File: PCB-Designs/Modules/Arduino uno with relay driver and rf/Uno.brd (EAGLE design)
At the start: 157.2 x 94 mm, 54 parts, among them IC1 ATMEGA328, IC2 7805, Q1 12MHZ, T1 BC547, T2 BC547, T3 BC547, T4 BC547

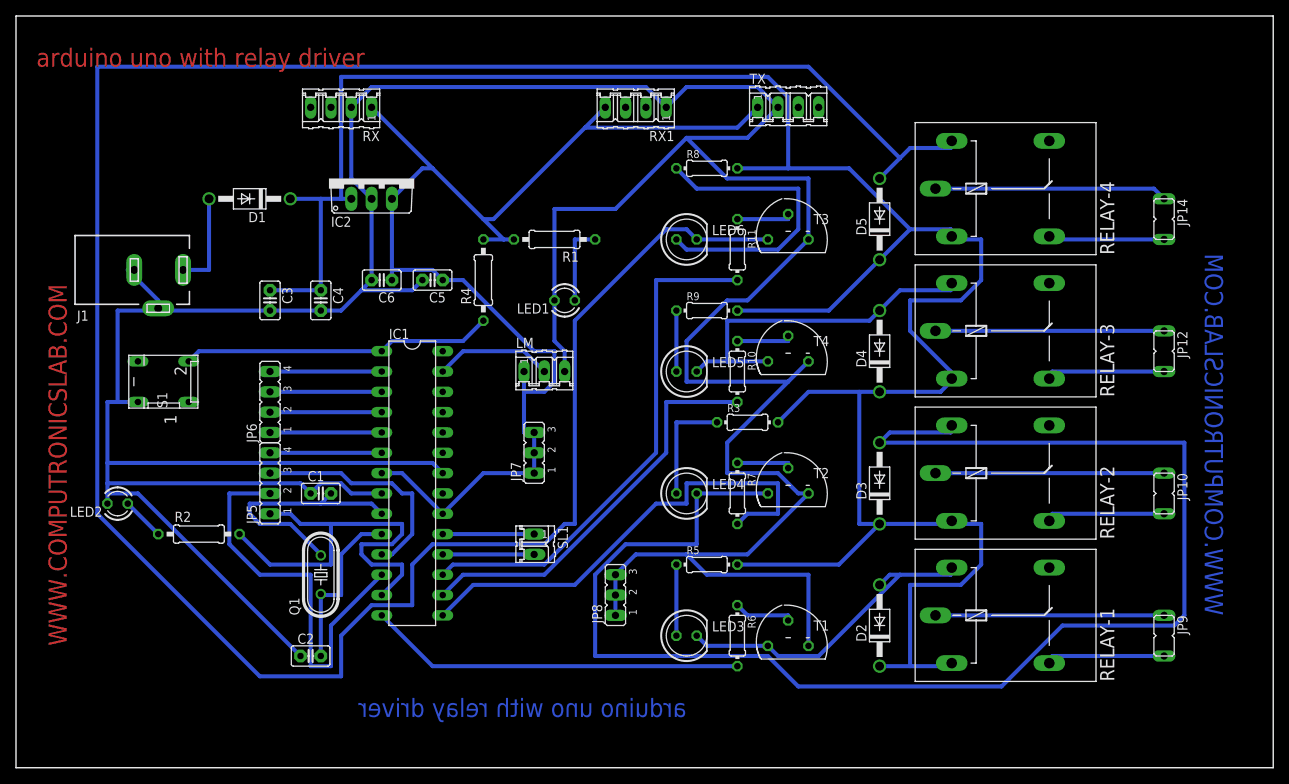
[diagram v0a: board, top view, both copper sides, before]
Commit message: 
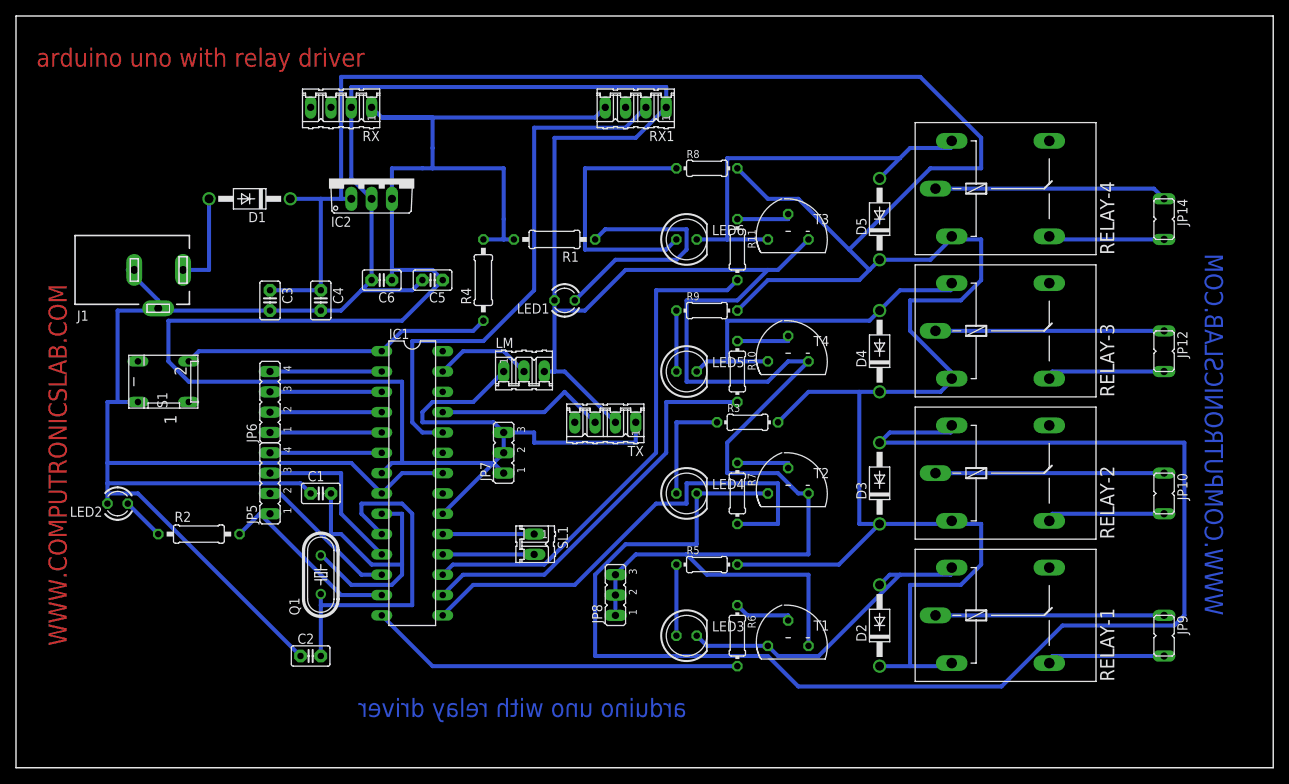
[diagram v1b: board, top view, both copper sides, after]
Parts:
- moved TX 45.5 mm to (77.5, 52.1), turned to 180 degrees
- moved JP7 3.81 mm to (64.8, 48.3)
- moved LM 2.54 mm to (67.3, 58.4)
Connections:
- net N$9: now also RX1.2
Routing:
- net N$58: track 309.1 -> 52.0 mm
- net N$4: track 157.5 -> 246.5 mm
- net N$9: track 0.00 -> 67.7 mm
- net N$7: track 304.2 -> 342.1 mm
- net N$19: track 51.2 -> 18.2 mm
- net N$21: track 53.7 -> 24.3 mm
- net N$11: track 0.00 -> 21.7 mm
- net N$6: track 10.2 -> 31.1 mm
- net N$2: track 21.5 -> 42.3 mm
- net N$20: track 28.8 -> 21.2 mm
- net N$1: track 31.2 -> 38.1 mm
- net N$48: track 38.2 -> 33.5 mm
- net N$55: track 473.2 -> 469.3 mm
- net N$8: track 14.8 -> 12.3 mm
- net N$57: track 64.7 -> 64.0 mm
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
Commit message: 
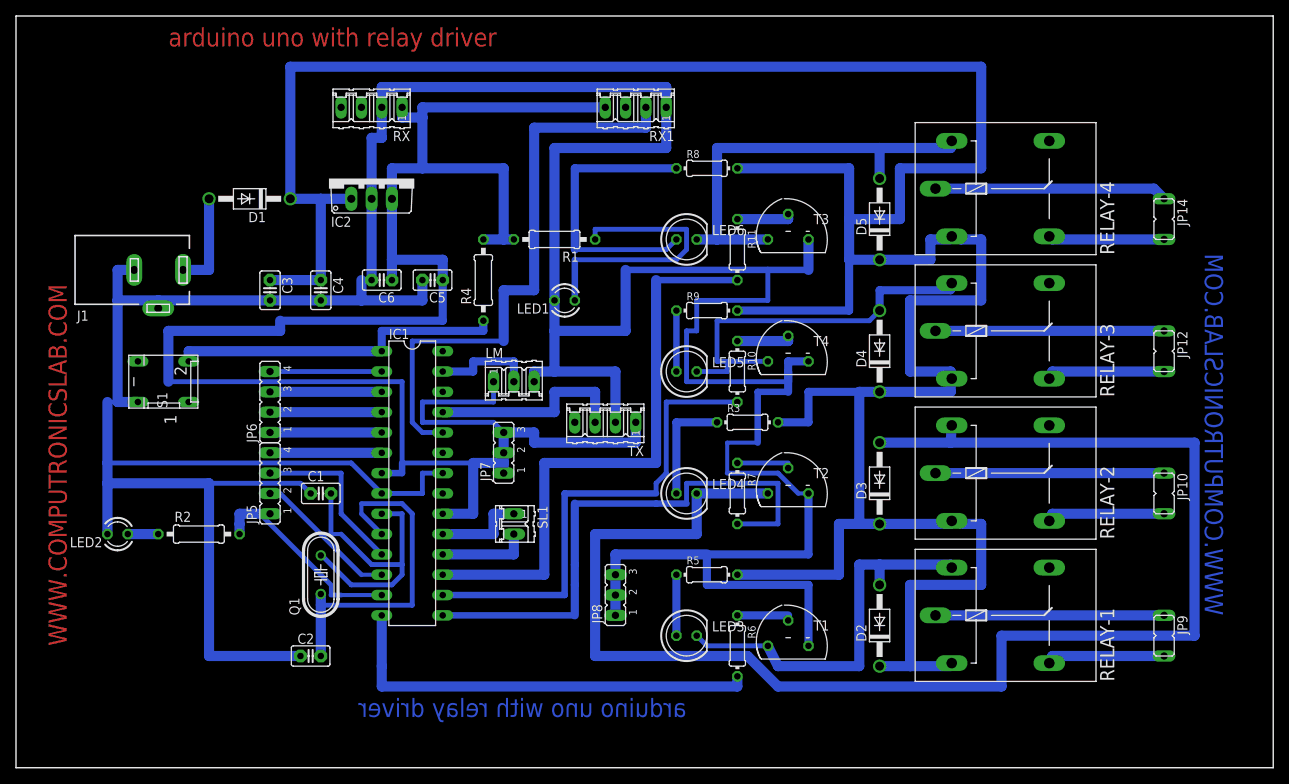
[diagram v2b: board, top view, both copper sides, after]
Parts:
- moved LED2 3.81 mm to (16.5, 38.1)
- moved RX 3.81 mm to (48.3, 91.4)
- moved SL1 3.59 mm to (66.0, 39.4)
- moved LM 1.80 mm to (66.0, 57.1)
- moved R6 1.27 mm to (94.0, 24.1)
- moved C3 1.27 mm to (35.6, 68.6)
- moved C4 1.27 mm to (41.9, 68.6)
- moved R5 1.27 mm to (90.2, 33.0)
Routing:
- net N$7: track 342.1 -> 378.3 mm
- net N$55: track 469.3 -> 497.7 mm
- net N$57: track 64.0 -> 73.7 mm
- net N$56: track 50.5 -> 60.2 mm
- net N$28: track 41.0 -> 49.5 mm
- net N$59: track 60.4 -> 68.6 mm
- net N$41: track 47.1 -> 54.6 mm
- net N$9: track 67.7 -> 72.9 mm
- net N$43: track 44.9 -> 49.7 mm
- net N$11: track 21.7 -> 25.4 mm
- net N$6: track 31.1 -> 34.8 mm
- net N$31: track 38.9 -> 41.9 mm
- net N$48: track 33.5 -> 36.1 mm
- net N$21: track 24.3 -> 26.5 mm
- net N$58: track 52.0 -> 54.2 mm
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
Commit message: 
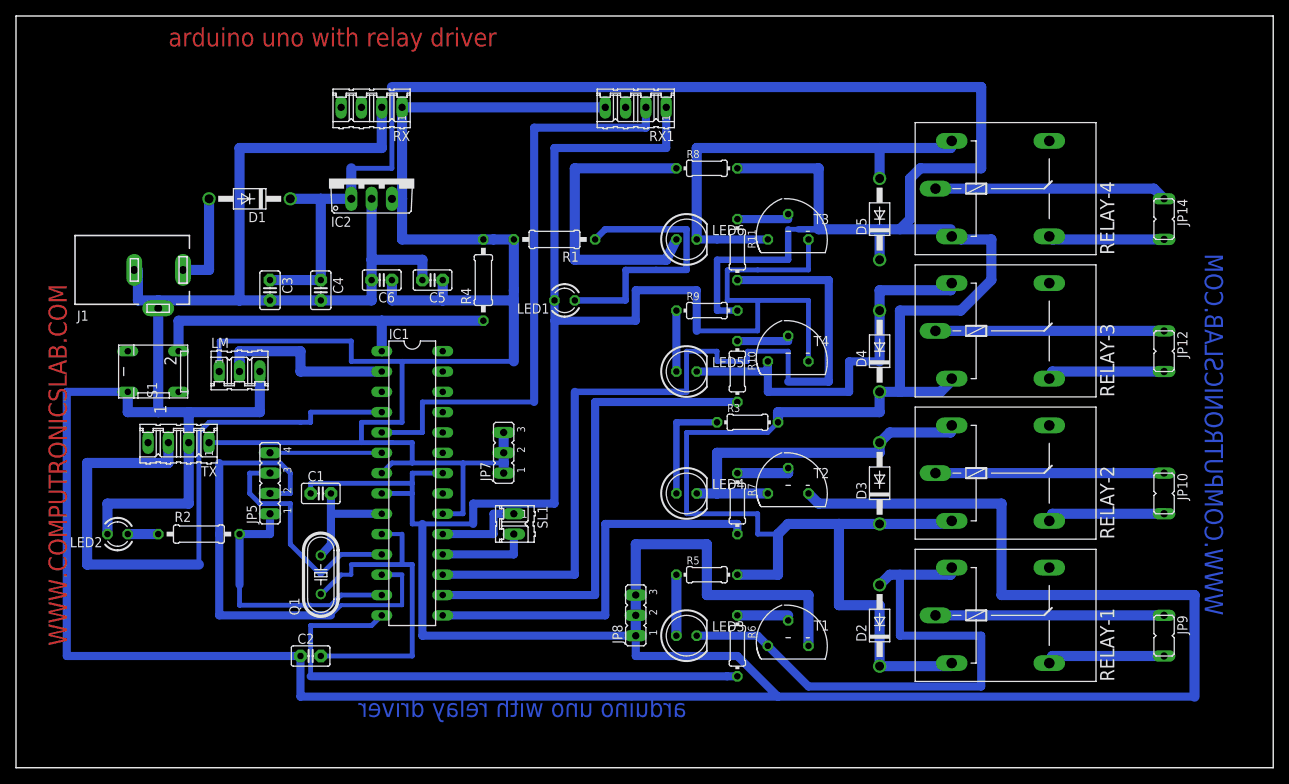
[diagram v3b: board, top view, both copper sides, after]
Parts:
- removed JP6: (no value), jumper:JP4
- moved TX 53.4 mm to (24.1, 49.5)
- moved LM 34.3 mm to (31.8, 58.4)
- moved JP8 3.59 mm to (81.3, 27.9)
- moved S1 1.80 mm to (21.6, 58.4)
- moved R7 1.27 mm to (94.0, 41.9)
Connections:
- removed net N$14: IC1.5, JP6.1
- removed net N$15: IC1.2, JP6.4
- removed net N$16: IC1.3, JP6.3
- removed net N$17: IC1.4, JP6.2
- net N$11: now also IC1.4; no longer IC1.25
- net N$8: now also IC1.2; no longer IC1.27
- net N$9: now also IC1.5; no longer IC1.24
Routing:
- net N$55: track 497.7 -> 714.3 mm
- net N$42: track 190.4 -> 45.9 mm
- net N$11: track 25.4 -> 80.5 mm
- net N$19: track 18.2 -> 63.3 mm
- net N$4: track 246.9 -> 210.1 mm
- net N$57: track 73.7 -> 106.7 mm
- net N$1: track 38.1 -> 14.6 mm
- net N$28: track 49.5 -> 72.6 mm
- net N$59: track 68.6 -> 49.5 mm
- net N$41: track 54.6 -> 69.1 mm
- net N$17: track 14.0 -> 0.00 mm
- net N$16: track 14.0 -> 0.00 mm
- net N$15: track 14.0 -> 0.00 mm
- net N$14: track 14.0 -> 0.00 mm
- net N$8: track 12.7 -> 22.9 mm
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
